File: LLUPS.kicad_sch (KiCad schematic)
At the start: 37 parts, among them J1 USB_C, J2 Output, J3 Debug, Q1 FS8205A, U1 USBLC6-2SC6, U2 BQ24072, U3 HY2113-KB5B, U4 MT3608, U5 AP2112K-3.3, U6 LN61CN3302MR-G

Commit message: Fix battery holder footprint to match BOM
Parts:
- BT1, BT2: footprint Battery:BatteryHolder_Keystone_1042_1x18650 -> LLUPS:BatteryHolder_MYOUNG_BH-18650-A1AJ006
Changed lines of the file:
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@@
 			(effects (font (size 1.27 1.27)))
 		)
-		(property "Footprint" "Battery:BatteryHolder_Keystone_1042_1x18650"
+		(property "Footprint" "LLUPS:BatteryHolder_MYOUNG_BH-18650-A1AJ006"
 			(at 260 70 0)
 			(effects (font (size 1.27 1.27)) (hide yes))
@@
 			(effects (font (size 1.27 1.27)))
 		)
-		(property "Footprint" "Battery:BatteryHolder_Keystone_1042_1x18650"
+		(property "Footprint" "LLUPS:BatteryHolder_MYOUNG_BH-18650-A1AJ006"
 			(at 280 70 0)
 			(effects (font (size 1.27 1.27)) (hide yes))

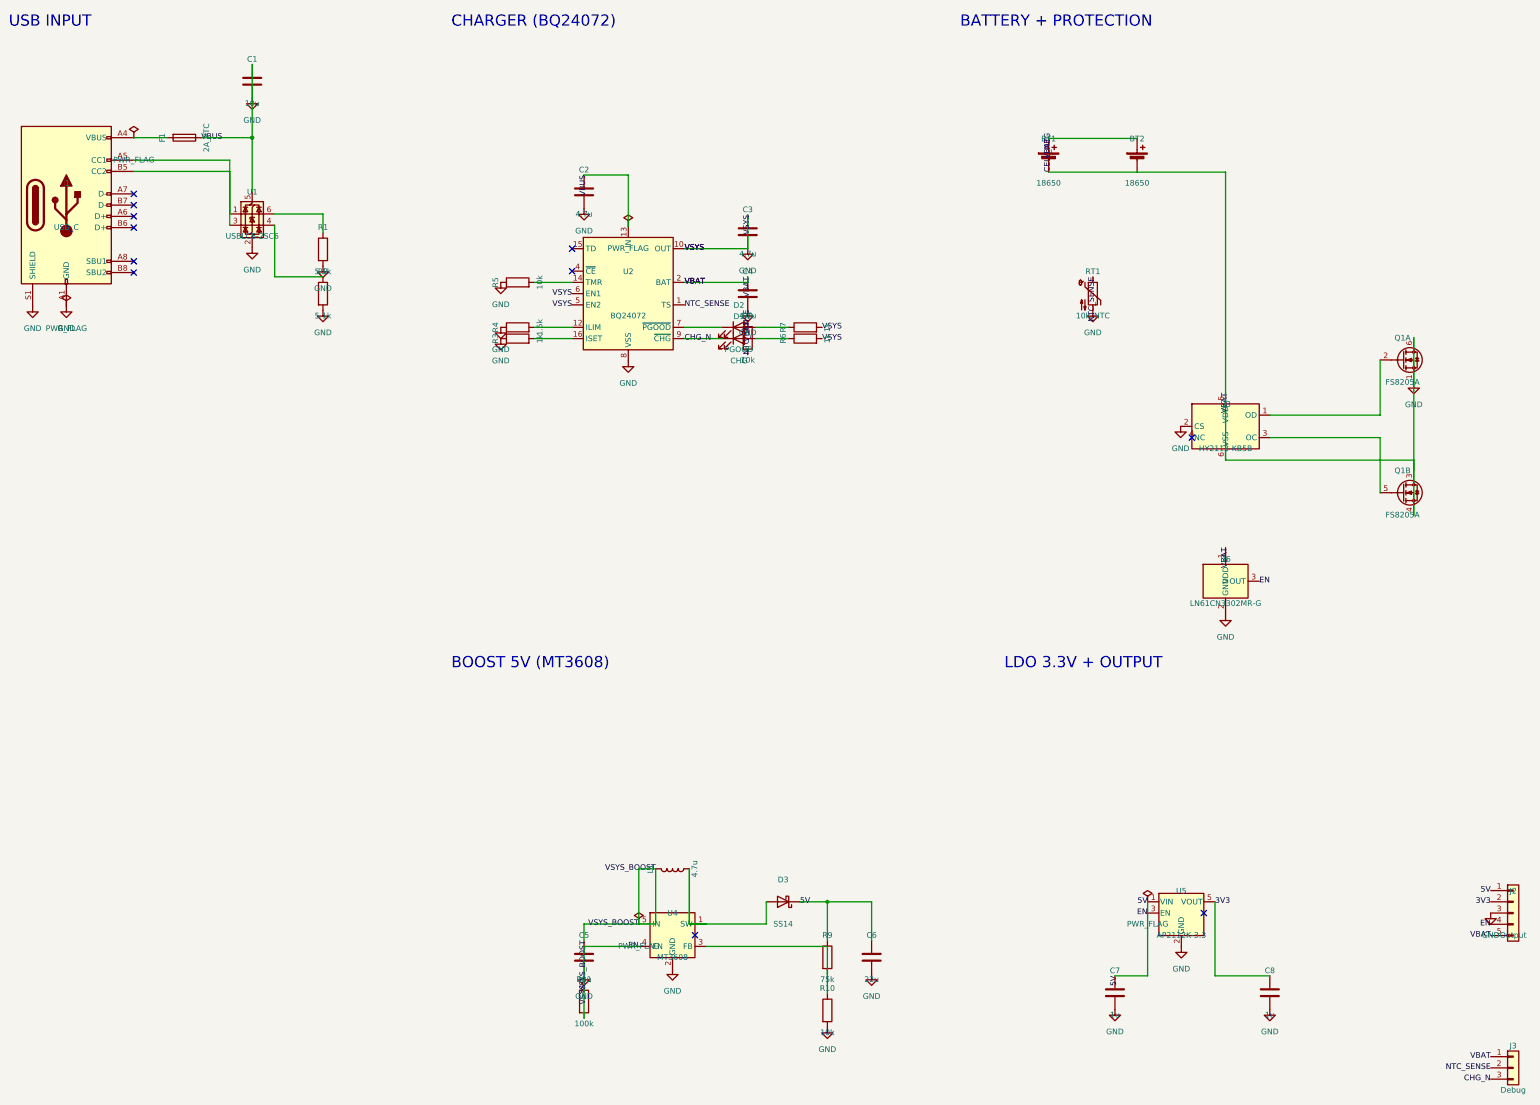
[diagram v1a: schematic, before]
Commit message: Add generalized KiCad group labeling and schematic splitting
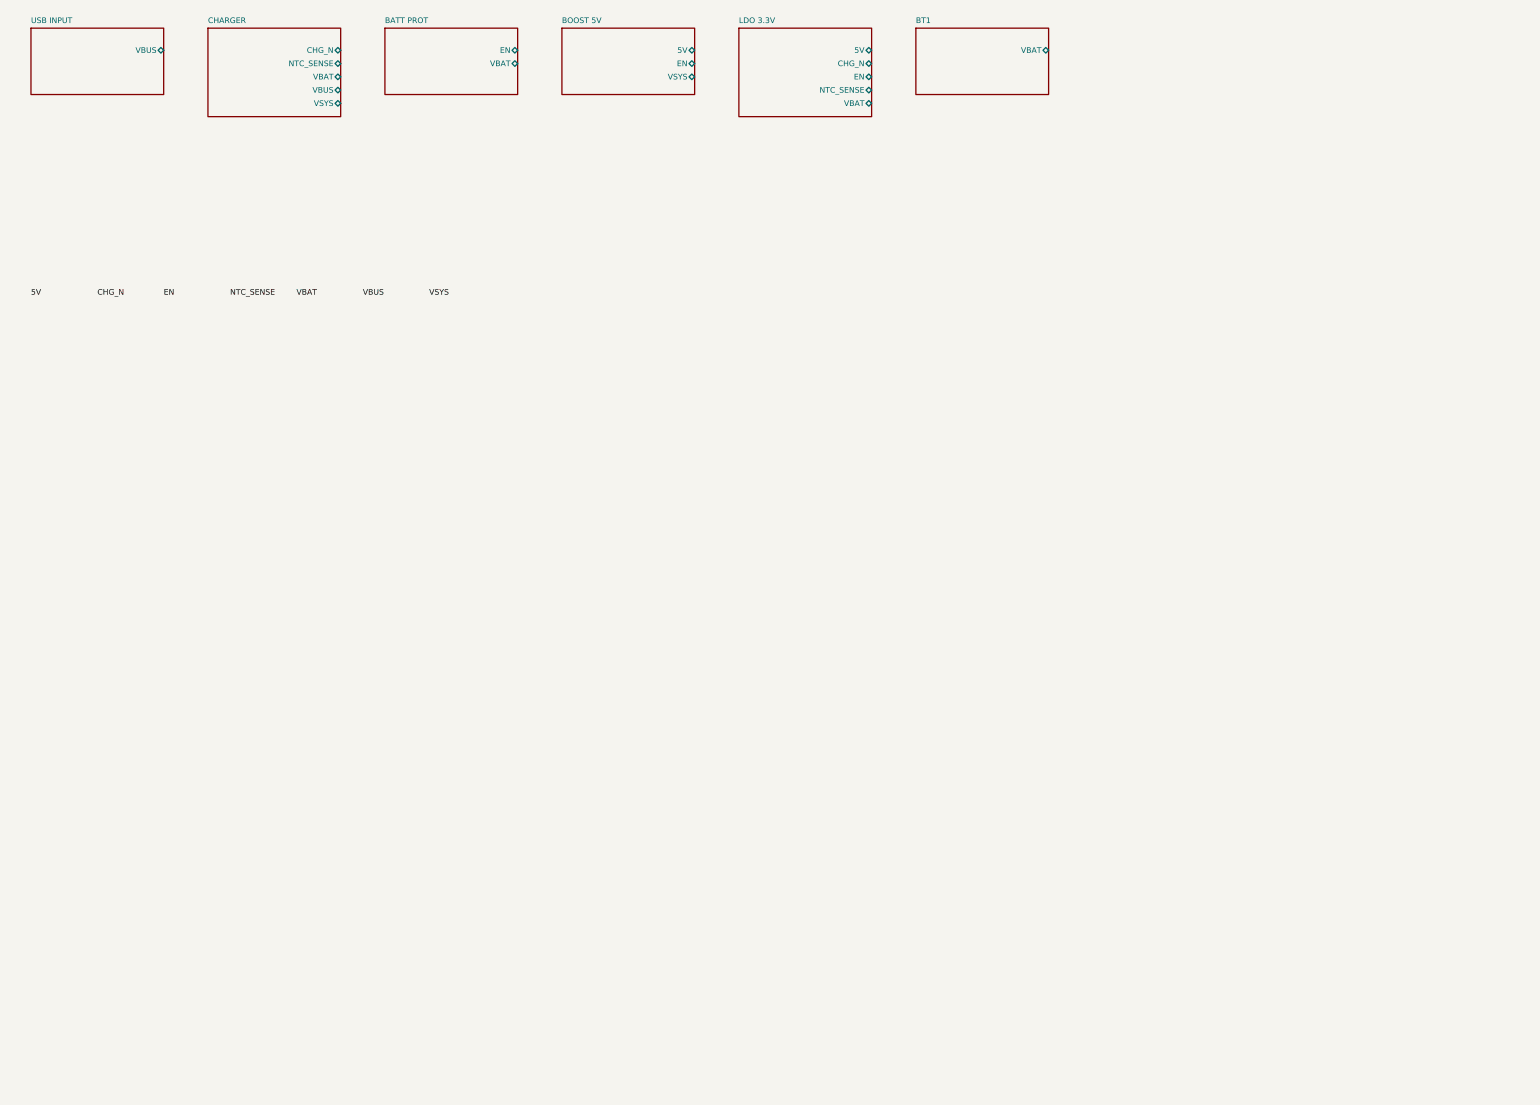
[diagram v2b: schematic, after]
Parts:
- removed BT1, BT2: 18650, LLUPS:BatteryHolder_MYOUNG_BH-18650-A1AJ006, symbol Device:Battery_Cell
- removed C1, C5: 10u, Capacitor_SMD:C_0805_2012Metric, symbol Device:C
- removed C2, C3, C4: 4.7u, Capacitor_SMD:C_0402_1005Metric, symbol Device:C
- removed C6: 22u, Capacitor_SMD:C_0805_2012Metric, symbol Device:C
- removed C7, C8: 1u, Capacitor_SMD:C_0402_1005Metric, symbol Device:C
- removed D1: CHG, LED_SMD:LED_0603_1608Metric, symbol Device:LED
- removed D2: PGOOD, LED_SMD:LED_0603_1608Metric, symbol Device:LED
- removed D3: SS14, Diode_SMD:D_SMA, symbol Device:D_Schottky
- removed F1: 2A_PTC, Fuse:Fuse_0805_2012Metric, symbol Device:Fuse
- removed J1: USB_C, Connector_USB:USB_C_Receptacle_GCT_USB4085, symbol Connector:USB_C_Receptacle_USB2.0_16P
- removed J2: Output, Connector_PinHeader_2.54mm:PinHeader_1x05_P2.54mm_Vertical, symbol Connector_Generic:Conn_01x05
- removed J3: Debug, Connector_PinHeader_2.54mm:PinHeader_1x03_P2.54mm_Vertical, symbol Connector_Generic:Conn_01x03
- removed L1: 4.7u, Inductor_SMD:L_0805_2012Metric, symbol Device:L
- removed Q1: FS8205A, Package_TO_SOT_SMD:SOT-23-6, symbol Transistor_FET:Q_Dual_NMOS_S1G1D2S2G2D1
- removed R1, R2: 5.1k, Resistor_SMD:R_0402_1005Metric, symbol Device:R
- removed R10, R5, R8: 10k, Resistor_SMD:R_0402_1005Metric, symbol Device:R
- removed R11: 100k, Resistor_SMD:R_0402_1005Metric, symbol Device:R
- removed R3, R6, R7: 1k, Resistor_SMD:R_0402_1005Metric, symbol Device:R
- removed R4: 1.5k, Resistor_SMD:R_0402_1005Metric, symbol Device:R
- removed R9: 75k, Resistor_SMD:R_0402_1005Metric, symbol Device:R
- removed RT1: 10k_NTC, Resistor_SMD:R_0402_1005Metric, symbol Device:Thermistor_NTC
- removed U1: USBLC6-2SC6, Package_TO_SOT_SMD:SOT-23-6, symbol Power_Protection:USBLC6-2SC6
- removed U2: BQ24072, Package_DFN_QFN:VQFN-16-1EP_3.5x3.5mm_P0.5mm_EP2.1x2.1mm, symbol Battery_Management:BQ24072RGT
- removed U3: HY2113-KB5B, Package_TO_SOT_SMD:SOT-23-6, symbol Battery_Management:HY2113
- removed U4: MT3608, Package_TO_SOT_SMD:SOT-23-6, symbol Regulator_Switching:MT3608
- removed U5: AP2112K-3.3, Package_TO_SOT_SMD:SOT-23-5, symbol Regulator_Linear:AP2112K-3.3
- removed U6: LN61CN3302MR-G, Package_TO_SOT_SMD:SOT-23-3, symbol Supervisor:LN61C
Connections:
- no-connect marks 11 -> 0
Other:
- added sheet BATT PROT (BATT_PROT.kicad_sch)
- added sheet BOOST 5V (BOOST_5V.kicad_sch)
- added sheet BT1 (BT1.kicad_sch)
- added sheet CHARGER (CHARGER.kicad_sch)
- added sheet LDO 3.3V (LDO_3_3V.kicad_sch)
- added sheet USB INPUT (USB_INPUT.kicad_sch)
- note removed: "BATTERY + PROTECTION"
- note removed: "BOOST 5V (MT3608)"
- note removed: "CHARGER (BQ24072)"
- note removed: "LDO 3.3V + OUTPUT"
- note removed: "USB INPUT"
